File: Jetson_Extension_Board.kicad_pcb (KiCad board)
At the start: 2 copper layers, 93.8 x 78.5 mm, 26 parts, among them J1 I2C_2 DEBUG, J10 TBP03R2-350-03BE, J11 ST DEBUG, J12 TBP03R2-350-03BE, J13 TBP03R2-350-03BE, J14 Conn_01x06_Pin, J15 Conn_01x04_Pin, J2 TBP03R2-350-03BE, J3 TBP03R2-350-03BE, J4 TBP03R2-350-03BE, J5 TBP03R2-350-03BE, J6 40_Pin_Jetson_Connector, J7 TBP03R2-350-03BE, J8 TBP03R2-350-03BE, J9 TBP03R2-350-03BE, SW1 SW_Push_DPDT, U2 74LV14, U4 ADS1115IDGS

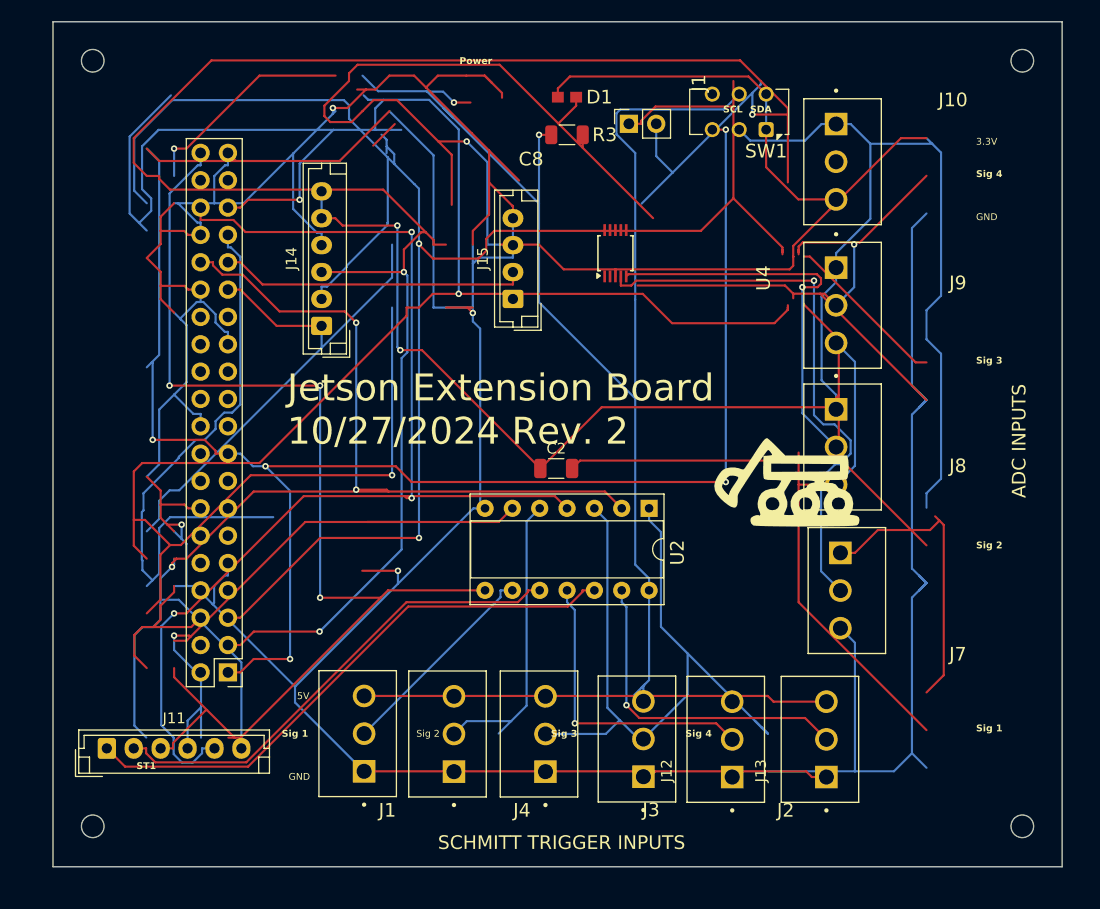
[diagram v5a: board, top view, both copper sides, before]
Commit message: added connectors for pots and compacted further
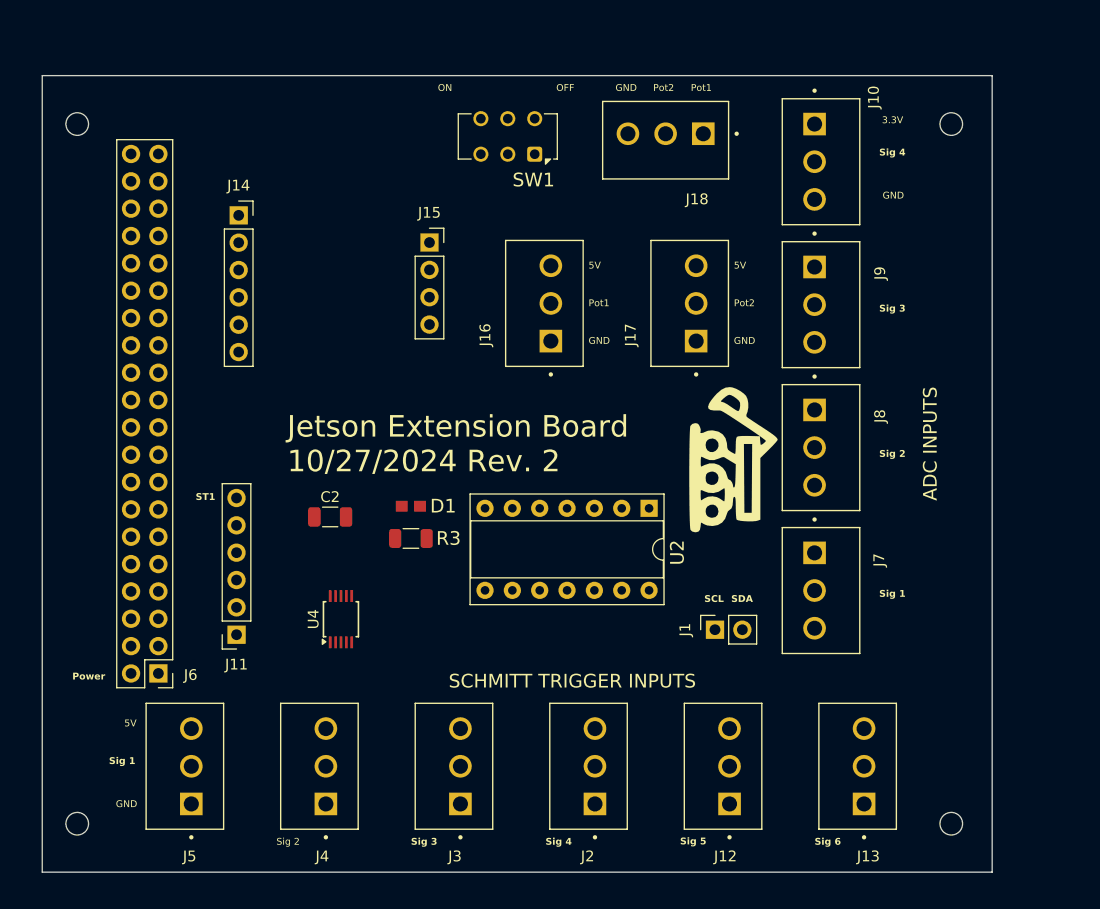
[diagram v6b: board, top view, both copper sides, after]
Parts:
- added J16: Pot1, TBP03R2_350_03BE(1):CUI_TBP03R2-350-03BE, F.Cu at (134.0, 97.2)
- added J17: Pot2, TBP03R2_350_03BE(1):CUI_TBP03R2-350-03BE, F.Cu at (147.5, 97.2)
- added J18: Pots_to_Nucleo, TBP03R2_350_03BE(1):CUI_TBP03R2-350-03BE, F.Cu at (148.2, 77.9)
- J11, J14: footprint Connector_JST:JST_EH_B6B-EH-A_1x06_P2.50mm_Vertical -> Connector_PinSocket_2.54mm:PinSocket_1x06_P2.54mm_Vertical
- J15: footprint Connector_JST:JST_EH_B4B-EH-A_1x04_P2.50mm_Vertical -> Connector_PinSocket_2.54mm:PinSocket_1x04_P2.54mm_Vertical
- moved J1 47.7 mm to (149.2, 124.0)
- moved U4 42.5 mm to (114.5, 123.0)
- moved D1 40.7 mm to (121.0, 112.5)
- moved R3 40.2 mm to (121.0, 115.5)
- moved SW1 21.6 mm to (132.5, 79.8)
- moved C2 21.5 mm to (113.5, 113.5)
- moved J5 16.3 mm to (100.6, 140.2)
- moved J11 16.0 mm to (104.8, 124.4), turned to 180 degrees
- moved J14 12.8 mm to (105.0, 85.5), turned to 0 degrees
- moved J4 12.3 mm to (113.1, 140.2)
- moved J15 9.36 mm to (122.7, 88.0), turned to 0 degrees
- moved H3 8.84 mm to (171.2, 77.0)
- moved J3 8.45 mm to (125.6, 140.2)
- moved H4 6.60 mm to (171.2, 142.0)
- moved J6 6.46 mm to (97.5, 128.0)
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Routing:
- net GND: track 600.9 -> 0.00 mm, vias 4 -> 0
- net /ADC/3.3V: track 225.5 -> 0.00 mm, vias 2 -> 0
- net COM 3: track 220.8 -> 0.00 mm, vias 3 -> 0
- net /I2C_2_SDA: track 192.2 -> 0.00 mm, vias 3 -> 0
- net /I2C_2_SCL: track 173.5 -> 0.00 mm, vias 2 -> 0
- net /SchmittTrigger(74LV14)/5V: track 170.8 -> 0.00 mm, vias 2 -> 0
- net 3.3V: track 145.5 -> 0.00 mm, vias 5 -> 0
- net ST 1: track 118.4 -> 0.00 mm, vias 3 -> 0
- net ST 2: track 107.1 -> 0.00 mm, vias 3 -> 0
- net ST 4: track 106.7 -> 0.00 mm, vias 3 -> 0
- net Net-(D1-Pad2): track 77.6 -> 0.00 mm, vias 1 -> 0
- net ST 3: track 57.7 -> 0.00 mm, vias 1 -> 0
- net /ADC/Signal 3: track 55.7 -> 0.00 mm, vias 1 -> 0
- net unconnected-(J6-Pin_33-Pad33): track 54.7 -> 0.00 mm
- net /SchmittTrigger(74LV14)/ST 6: track 52.9 -> 0.00 mm
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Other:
- board size 93.8 x 78.5 mm -> 88.2 x 74 mm
- board text added: "OFF"
- board text added: "ON"
- board text added: "Pot1"
- board text added: "Pot2"
- board text added: "Sig 5"
- board text added: "Sig 6"
- board text removed: "C8"
- board text removed: "J1"
- board text removed: "J10"
- board text removed: "J2"
- board text removed: "J3"
- board text removed: "J4"
- board text removed: "J7"
- board text removed: "J8"
- board text removed: "J9"
- board text removed: "U4"

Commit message: changed hole sizes, added labels, added ground plane, set trace width min
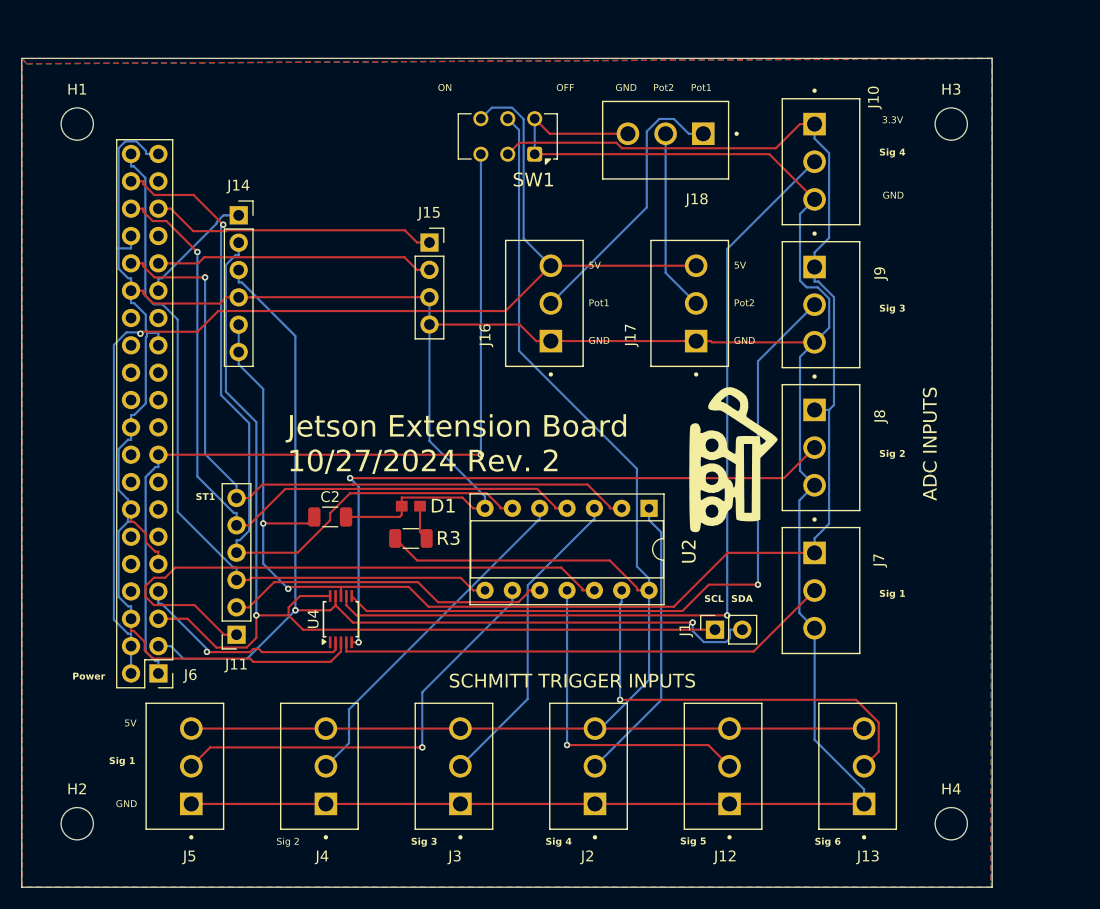
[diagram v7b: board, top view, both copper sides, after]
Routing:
- net GND: track 0.00 -> 356.3 mm
- net /ADC/3.3V: track 0.00 -> 158.2 mm, vias 0 -> 2
- net /SchmittTrigger(74LV14)/5V: track 0.00 -> 152.7 mm
- net 5V: track 0.00 -> 108.1 mm, vias 0 -> 1
- net /I2C_2_SCL: track 0.00 -> 97.3 mm, vias 0 -> 1
- net /I2C_2_SDA: track 0.00 -> 94.4 mm, vias 0 -> 2
- net /ADC/Signal 4: track 0.00 -> 82.1 mm, vias 0 -> 1
- net 3.3V: track 0.00 -> 79.5 mm, vias 0 -> 1
- net ST 3: track 0.00 -> 71.6 mm, vias 0 -> 1
- net ST 4: track 0.00 -> 68.1 mm
- net ST 2: track 0.00 -> 68.0 mm, vias 0 -> 1
- net /ADC/Signal 3: track 0.00 -> 67.5 mm, vias 0 -> 1
- net ST 1: track 0.00 -> 66.6 mm, vias 0 -> 1
- net /ADC/Signal 2: track 0.00 -> 60.5 mm, vias 0 -> 2
- net /SchmittTrigger(74LV14)/ST 6: track 0.00 -> 54.3 mm
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- added copper zone on B.Cu, net GND
- added copper zone on F.Cu, net GND
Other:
- board size 88.2 x 74 mm -> 90.2 x 77 mm

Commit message: alignment fixes
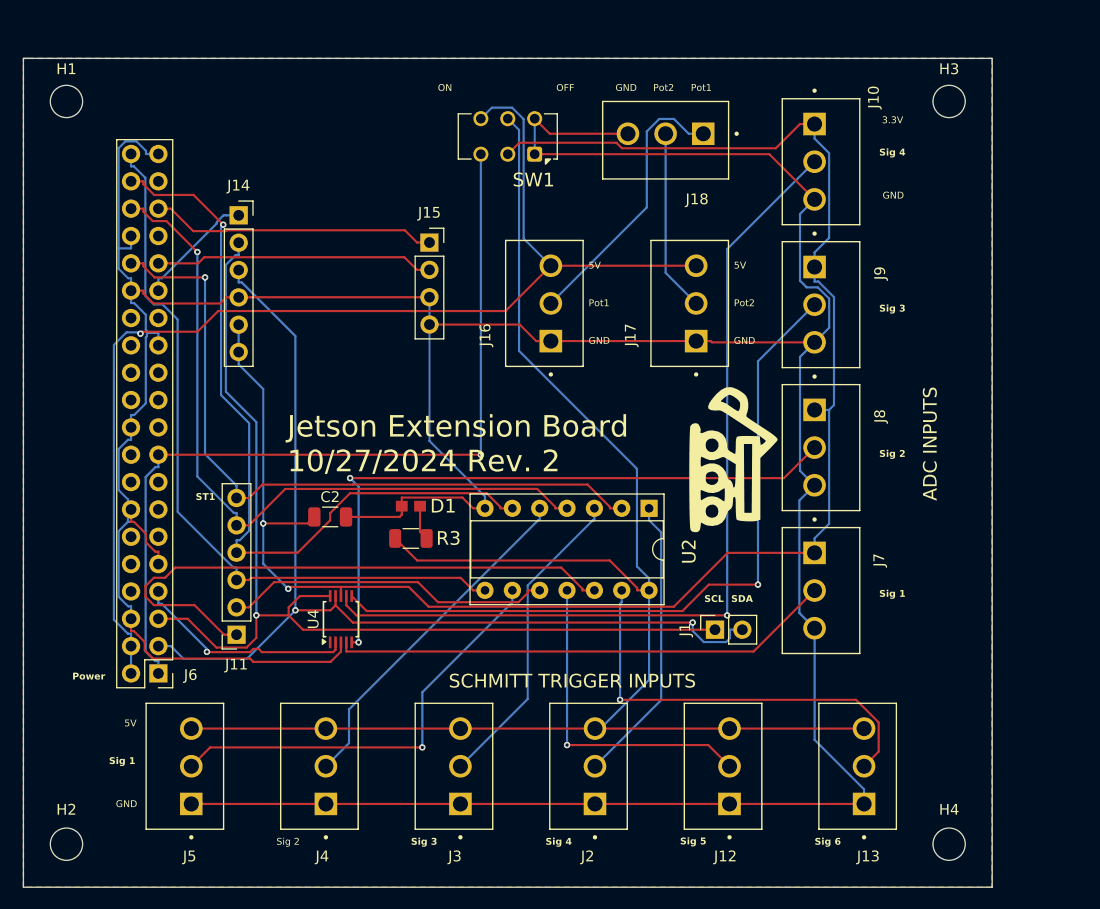
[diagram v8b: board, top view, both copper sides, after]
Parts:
- moved H1 2.33 mm to (89.0, 74.9)
- moved H2 2.15 mm to (89.0, 143.9)
- moved H3 2.11 mm to (171.0, 74.9)
- moved H4 1.91 mm to (171.0, 143.9)
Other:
- board size 90.2 x 77 mm -> 90 x 77 mm
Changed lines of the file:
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@@
 	(footprint "MountingHole:MountingHole_2.1mm"
 		(layer "F.Cu")
-		(at 171.2 142)
+		(at 171 143.9)
 		(descr "Mounting Hole 2.1mm, no annular")
 		(tags "mounting hole 2.1mm no annular")
@@
 	(footprint "MountingHole:MountingHole_2.1mm"
 		(layer "F.Cu")
-		(at 90 142)
+		(at 89 143.9)
 		(descr "Mounting Hole 2.1mm, no annular")
 		(tags "mounting hole 2.1mm no annular")
@@
 	(footprint "MountingHole:MountingHole_2.1mm"
 		(layer "F.Cu")
-		(at 171.2 77)
+		(at 171 74.9)
 		(descr "Mounting Hole 2.1mm, no annular")
 		(tags "mounting hole 2.1mm no annular")
 		(property "Reference" "H3"
-			(at 0 -3.2 0)
+			(at 0 -3 0)
 			(layer "F.SilkS")
 			(effects
@@
 	(footprint "MountingHole:MountingHole_2.1mm"
 		(layer "F.Cu")
-		(at 90 77)
+		(at 89 74.9)
 		(descr "Mounting Hole 2.1mm, no annular")
 		(tags "mounting hole 2.1mm no annular")
 		(property "Reference" "H1"
-			(at 0 -3.2 0)
+			(at 0 -3 0)
 			(layer "F.SilkS")
 			(effects
@@
 	)
 	(gr_rect
-		(start 84.85 70.9)
+		(start 85 70.9)
 		(end 175 147.9)
 		(stroke
@@
 		(min_thickness 0.25)
 		(filled_areas_thickness no)
-		(fill yes
+		(fill
 			(thermal_gap 0.5)
 			(thermal_bridge_width 0.5)
@@
 		(polygon
 			(pts
-				(xy 85.3 71.4) (xy 175 70.9) (xy 174.9 147.5) (xy 175 147.9) (xy 84.9 147.9) (xy 84.9 70.9)
+				(xy 85.4 70.9) (xy 175 70.9) (xy 175 147.5) (xy 175 147.9) (xy 85 147.9) (xy 85 70.9)
 			)
 		)
